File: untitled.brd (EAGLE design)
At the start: 81.3 x 56.8 mm, 12 parts

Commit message: added ground planes
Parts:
- added JP13, JP14, JP15: (no value), SparkFun:1X03
- moved JP12 39.5 mm to (2.54, 48.3), turned to 270 degrees
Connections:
- new net MS1: JP13.2, JP3.7, JP5.7, JP7.7
- new net MS2: JP14.2, JP3.6, JP5.6, JP7.6
- new net MS3: JP15.2, JP3.5, JP5.5, JP7.5
- net 5V: now also JP13.3, JP14.3, JP15.3
- net GND: now also JP1.12, JP13.1, JP14.1, JP15.1
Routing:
- net MS2: track 0.00 -> 92.8 mm, vias 0 -> 1
- net MS3: track 0.00 -> 83.3 mm
- net MS1: track 0.00 -> 82.3 mm, vias 0 -> 1
- net GND: track 81.7 -> 139.8 mm, vias 0 -> 1
- net GNDMOT: track 134.6 -> 81.5 mm
- net VMOT: track 106.6 -> 71.0 mm, vias 3 -> 0
- net 5V: track 141.4 -> 120.0 mm
- net ZSTP: track 46.3 -> 55.8 mm, vias 0 -> 3
- net YSTP: track 56.7 -> 50.1 mm
- net DISABLE: track 96.4 -> 101.0 mm, vias 0 -> 1
- net XSTP: track 33.7 -> 30.4 mm, vias 0 -> 1
- net ZDIR: vias 1 -> 2
- net XDIR: vias 1 -> 2
- added copper zone on layer 1, net GND
- added copper zone on layer 16, net GND

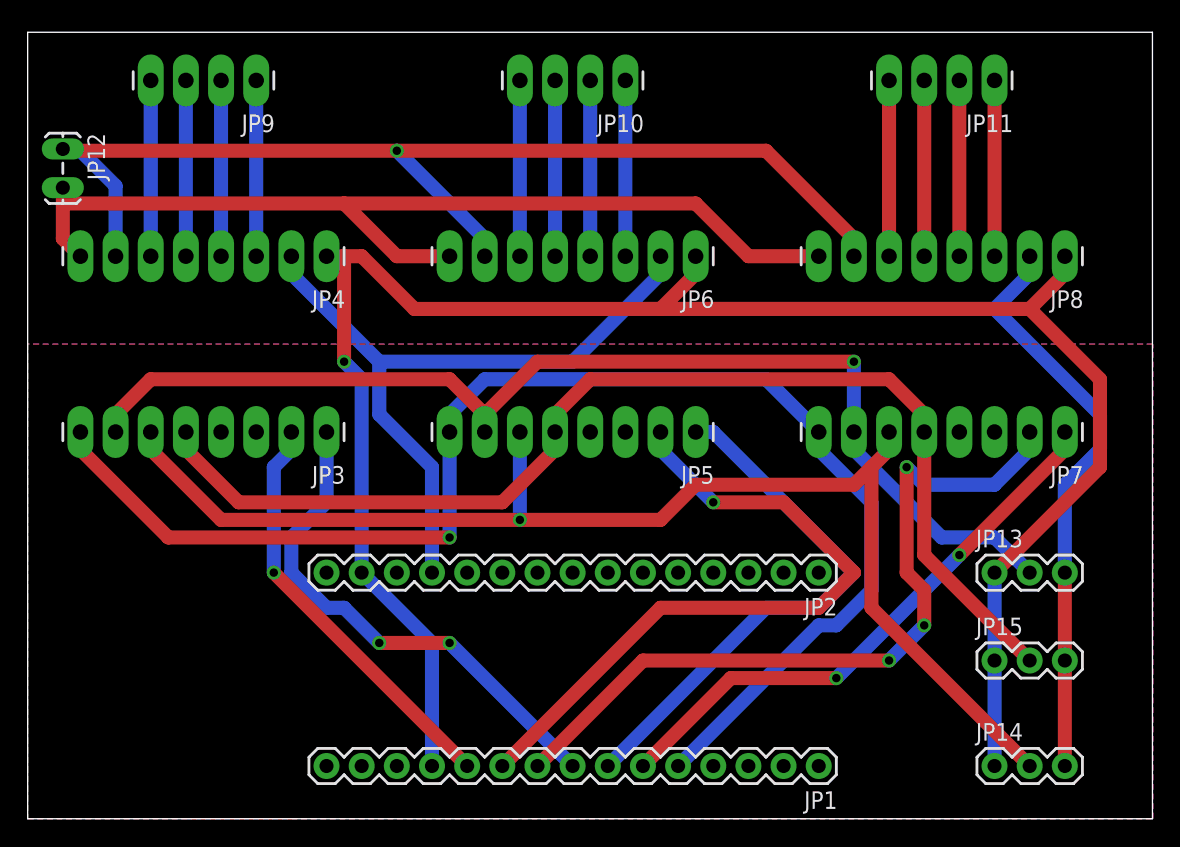
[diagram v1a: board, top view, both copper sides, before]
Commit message: connected sleep and rst, one was floating
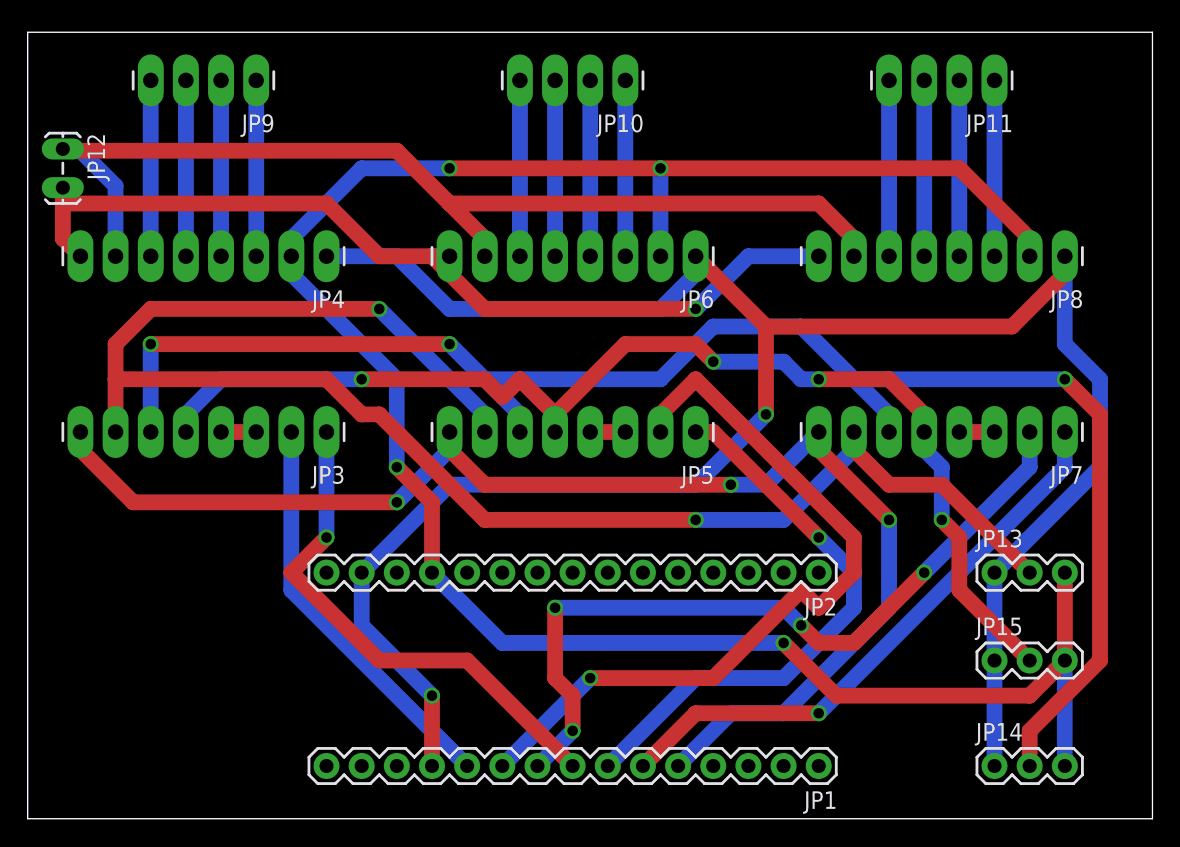
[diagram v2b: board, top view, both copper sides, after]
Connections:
- new net N$1: JP5.3, JP5.4
- new net N$14: JP7.3, JP7.4
- new net N$15: JP3.3, JP3.4
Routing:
- net 5V: track 120.0 -> 157.9 mm, vias 0 -> 4
- net MS1: track 82.3 -> 117.1 mm, vias 1 -> 2
- net MS2: track 92.8 -> 117.4 mm, vias 1 -> 3
- net GND: track 139.8 -> 159.6 mm, vias 1 -> 2
- net YSTP: track 50.1 -> 55.8 mm
- net GNDMOT: track 81.5 -> 76.1 mm, vias 1 -> 0
- net VMOT: track 71.0 -> 66.2 mm, vias 0 -> 1
- net DISABLE: track 101.0 -> 97.7 mm, vias 1 -> 3
- net N$15: track 0.00 -> 2.54 mm
- net N$1: track 0.00 -> 2.54 mm
- net N$14: track 0.00 -> 2.54 mm
- net YDIR: track 39.2 -> 40.7 mm, vias 0 -> 1
- net XSTP: track 30.4 -> 29.4 mm, vias 1 -> 0
- net MS3: track 83.3 -> 84.2 mm, vias 0 -> 4
- net ZDIR: track 41.2 -> 42.0 mm, vias 2 -> 1
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- removed copper zone on layer 1, net GND
- removed copper zone on layer 16, net GND

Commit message: added gnd plane and rerouted
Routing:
- added copper zone on layer 1, net GND
- added copper zone on layer 16, net GND
- added copper zone on layer 1, net GNDMOT
- added copper zone on layer 16, net GNDMOT
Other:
- board text added: "github.com/txjammer"
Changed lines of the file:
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@@
 <wire x1="81.26" y1="56.82" x2="0" y2="56.82" width="0" layer="20"/>
 <wire x1="0" y1="56.82" x2="0" y2="0" width="0" layer="20"/>
+<text x="1.27" y="7.62" size="1.778" layer="25">github.com/txjammer</text>
+<text x="78.74" y="48.26" size="1.778" layer="26" rot="MR0">github.com/txjammer</text>
 </plain>
 <attributes>
@@
 <via x="29.21" y="8.89" extent="1-16" drill="0.762"/>
 <via x="53.34" y="29.21" extent="1-16" drill="0.762"/>
+<polygon width="0.4064" layer="16" isolate="0.6096">
+<vertex x="0" y="33.02"/>
+<vertex x="81.28" y="33.02"/>
+<vertex x="81.28" y="0"/>
+<vertex x="0" y="0"/>
+</polygon>
+<polygon width="0.4064" layer="1" isolate="0.6096">
+<vertex x="0" y="33.02"/>
+<vertex x="81.28" y="33.02"/>
+<vertex x="81.28" y="0"/>
+<vertex x="0" y="0"/>
+</polygon>
 </signal>
 <signal name="YDIR">
@@
 <wire x1="57.15" y1="44.45" x2="59.69" y2="41.91" width="1.143" layer="1"/>
 <wire x1="30.48" y1="44.45" x2="57.15" y2="44.45" width="1.143" layer="1"/>
+<polygon width="0.4064" layer="16" isolate="0.6096">
+<vertex x="0" y="57.15"/>
+<vertex x="81.28" y="57.15"/>
+<vertex x="81.28" y="34.29"/>
+<vertex x="0" y="34.29"/>
+</polygon>
+<polygon width="0.4064" layer="1" isolate="0.6096">
+<vertex x="0" y="57.15"/>
+<vertex x="81.28" y="57.15"/>
+<vertex x="81.28" y="34.29"/>
+<vertex x="0" y="34.29"/>
+</polygon>
 </signal>
 <signal name="N$2">

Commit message: left design files
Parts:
- added JP16, JP17, JP18: (no value), SparkFun:1X02_LOCK_LONGPADS
- moved JP14 7.62 mm to (69.8, 11.4)
- moved JP15 7.62 mm to (69.8, 3.81)
- moved JP12 1.27 mm to (2.54, 49.5)
- moved JP13 1.27 mm to (69.8, 19.1)
- moved JP2 1.27 mm to (57.1, 19.1)
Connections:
- new net SPINDLE_EN: JP1.1
- new net SPIN_DIR: JP2.1
- net 5V: now also JP16.1, JP17.1, JP18.1
- net XLIM: now also JP16.2
- net YLIM: now also JP17.2
- net ZLIM: now also JP18.2
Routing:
- net GNDMOT: track 76.1 -> 0.00 mm
- net XLIM: track 0.00 -> 63.8 mm, vias 0 -> 4
- net YLIM: track 0.00 -> 50.4 mm, vias 0 -> 3
- net ZLIM: track 0.00 -> 49.9 mm, vias 0 -> 2
- net MS1: track 117.1 -> 78.7 mm
- net MS2: track 117.4 -> 83.3 mm, vias 3 -> 2
- net GND: track 159.6 -> 136.6 mm, vias 2 -> 0
- net MS3: track 84.2 -> 95.8 mm, vias 4 -> 1
- net ZSTP: track 56.2 -> 46.3 mm, vias 4 -> 2
- net VMOT: track 66.2 -> 73.7 mm, vias 1 -> 0
- net YSTP: track 55.8 -> 50.1 mm
- net 5V: track 157.9 -> 162.0 mm, vias 4 -> 0
- net DISABLE: track 97.7 -> 100.7 mm, vias 3 -> 2
- net YDIR: track 40.7 -> 39.2 mm, vias 1 -> 0
- net XSTP: track 29.4 -> 30.4 mm, vias 0 -> 2
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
